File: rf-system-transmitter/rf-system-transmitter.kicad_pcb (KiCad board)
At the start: 4 copper layers, 45 x 49.5 mm, 52 parts, among them IC1 nRF905, IC2 MCP1700T-3302E_TT, J1 Battery input, J2 CONREVSMA001-G, J3 SWD, SW1 SW_Push, U1 STM32F103C8Tx, X1 16MHZ, X2 16MHZ

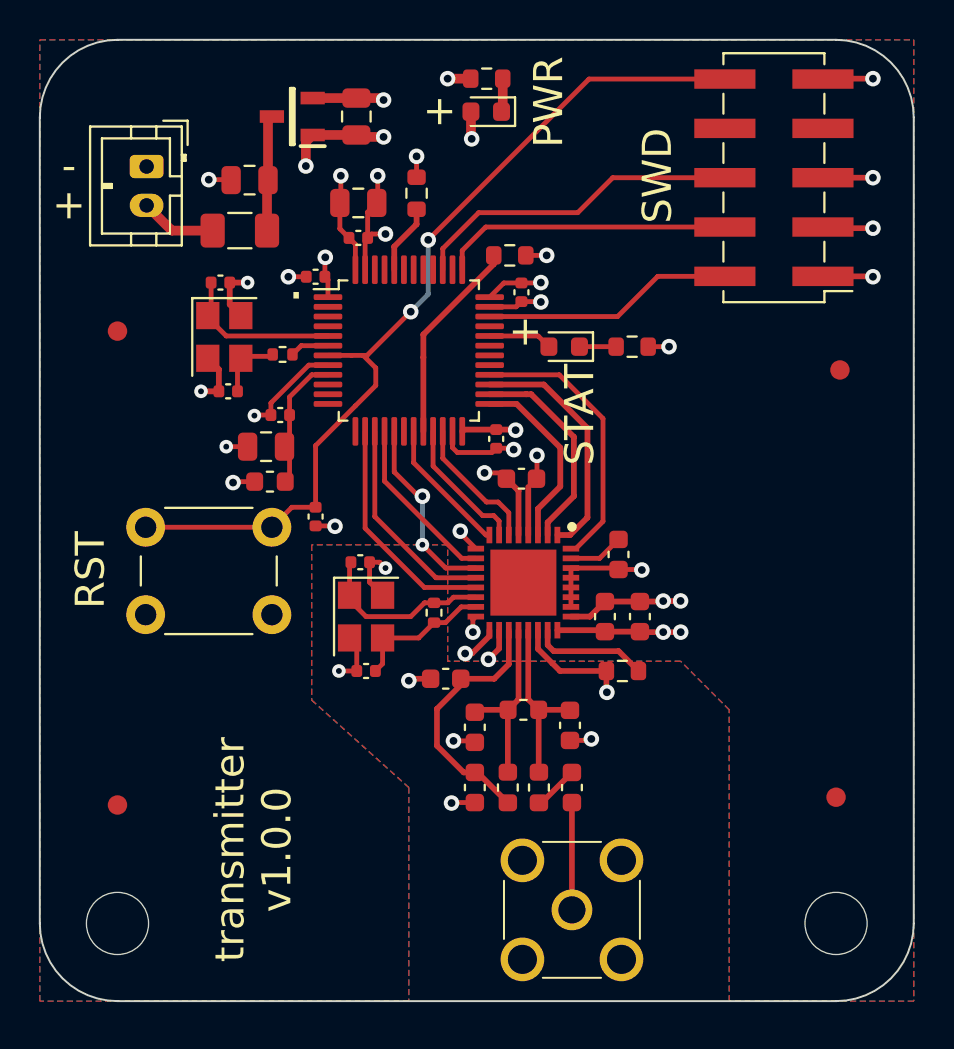
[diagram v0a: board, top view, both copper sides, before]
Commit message: add silkscreen, fiducials and tooling holes
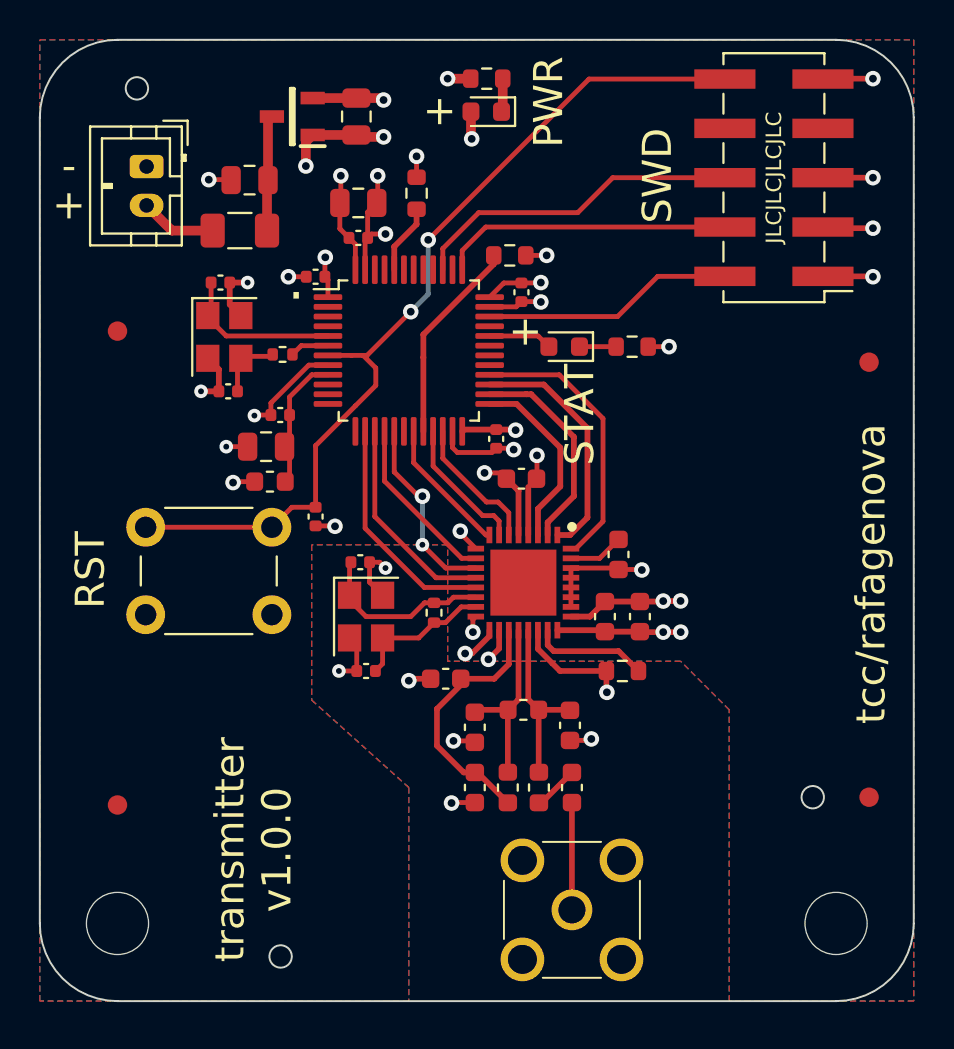
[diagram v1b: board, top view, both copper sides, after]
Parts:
- moved FID4 1.70 mm to (88.7, 61.0)
- moved FID2 1.55 mm to (88.7, 38.6)
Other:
- outline, holes or cut-outs redrawn
- board text added: "JLCJLCJLCJLC"
- board text added: "tcc/rafagenova"
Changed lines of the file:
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@@
   )
   (footprint "Fiducial:Fiducial_1mm_Mask2mm" (layer "F.Cu")
-    (at 87.2 39)
+    (at 88.7 38.6)
     (descr "Circular Fiducial, 1mm bare copper, 2mm soldermask opening (Level A)")
     (tags "fiducial")
@@
   )
   (footprint "Fiducial:Fiducial_1mm_Mask2mm" (layer "F.Cu")
-    (at 87 61)
+    (at 88.7 61)
     (descr "Circular Fiducial, 1mm bare copper, 2mm soldermask opening (Level A)")
     (tags "fiducial")
@@
     )
   )
+  (gr_circle locked (center 58.4 69.2) (end 58.976 69.2) (layer "Edge.Cuts") (width 0.1) (fill none))
   (gr_arc (start 46 26) (mid 47.171573 23.171573) (end 50 22) (layer "Edge.Cuts") (width 0.1))
   (gr_line (start 91 26) (end 91 67.5) (layer "Edge.Cuts") (width 0.1))
   (gr_line (start 87 71.5) (end 50 71.5) (layer "Edge.Cuts") (width 0.1))
   (gr_arc (start 87 22) (mid 89.828427 23.171573) (end 91 26) (layer "Edge.Cuts") (width 0.1))
+  (gr_circle locked (center 51 24.5) (end 51.576 24.5) (layer "Edge.Cuts") (width 0.1) (fill none))
   (gr_line (start 46 67.5) (end 46 26) (layer "Edge.Cuts") (width 0.1))
   (gr_arc (start 50 71.5) (mid 47.171573 70.328427) (end 46 67.5) (layer "Edge.Cuts") (width 0.1))
   (gr_line (start 50 22) (end 87 22) (layer "Edge.Cuts") (width 0.1))
+  (gr_circle (center 85.8 61) (end 86.376 61) (layer "Edge.Cuts") (width 0.1) (fill none))
   (gr_arc (start 91 67.5) (mid 89.828427 70.328427) (end 87 71.5) (layer "Edge.Cuts") (width 0.1))
   (gr_text "transmitter\nv1.0.0" (at 57 63.7 90) (layer "F.SilkS")
@@
     (effects (font (size 2 2) (thickness 0.3)))
   )
+  (gr_text "tcc/rafagenova" (at 88.8 49.5 90) (layer "F.SilkS")
+    (effects (font (size 1.5 1.5) (thickness 0.3)))
+  )
   (gr_text "PWR" (at 72.2 25.2 90) (layer "F.SilkS")
     (effects (font (size 1.5 1.5) (thickness 0.3)))
@@
     (effects (font (size 1.5 1.5) (thickness 0.3)))
   )
+  (gr_text "JLCJLCJLCJLC" (at 83.8 29.1 90) (layer "F.SilkS")
+    (effects (font (size 0.8 0.8) (thickness 0.15)))
+  )
   (gr_text "+" (at 66.6375 25.7 270) (layer "F.SilkS")

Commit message: adding LCSC Part # and small PCB modifs
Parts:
- C12: value 2.2p/0603 -> 33p/0603
- FB1: value 100@100MHz/0603 -> 100@100MHz/0805; footprint Inductor_SMD:L_0603_1608Metric -> Inductor_SMD:L_0805_2012Metric
- moved FB1 0.25 mm to (57.6, 44.8)
- moved C21 0.15 mm to (57.6, 42.8)
- moved SW1 0.15 mm to (51.5, 47.2)
- moved C22 0.12 mm to (58.4, 41.2)
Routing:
- net GND: track 82.5 -> 88.9 mm, vias 34 -> 62
